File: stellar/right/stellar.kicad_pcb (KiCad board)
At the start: 2 copper layers, 158 x 119.2 mm, 100 parts, among them J1 Battery+, J2 Battery, J3 Battery-, J4 OLED, SW1 SW_Push_45deg, SW10 SW_Push_45deg, SW11 SW_Push_45deg, SW12 SW_Push_45deg, SW13 SW_Push_45deg, SW14 SW_Push_45deg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

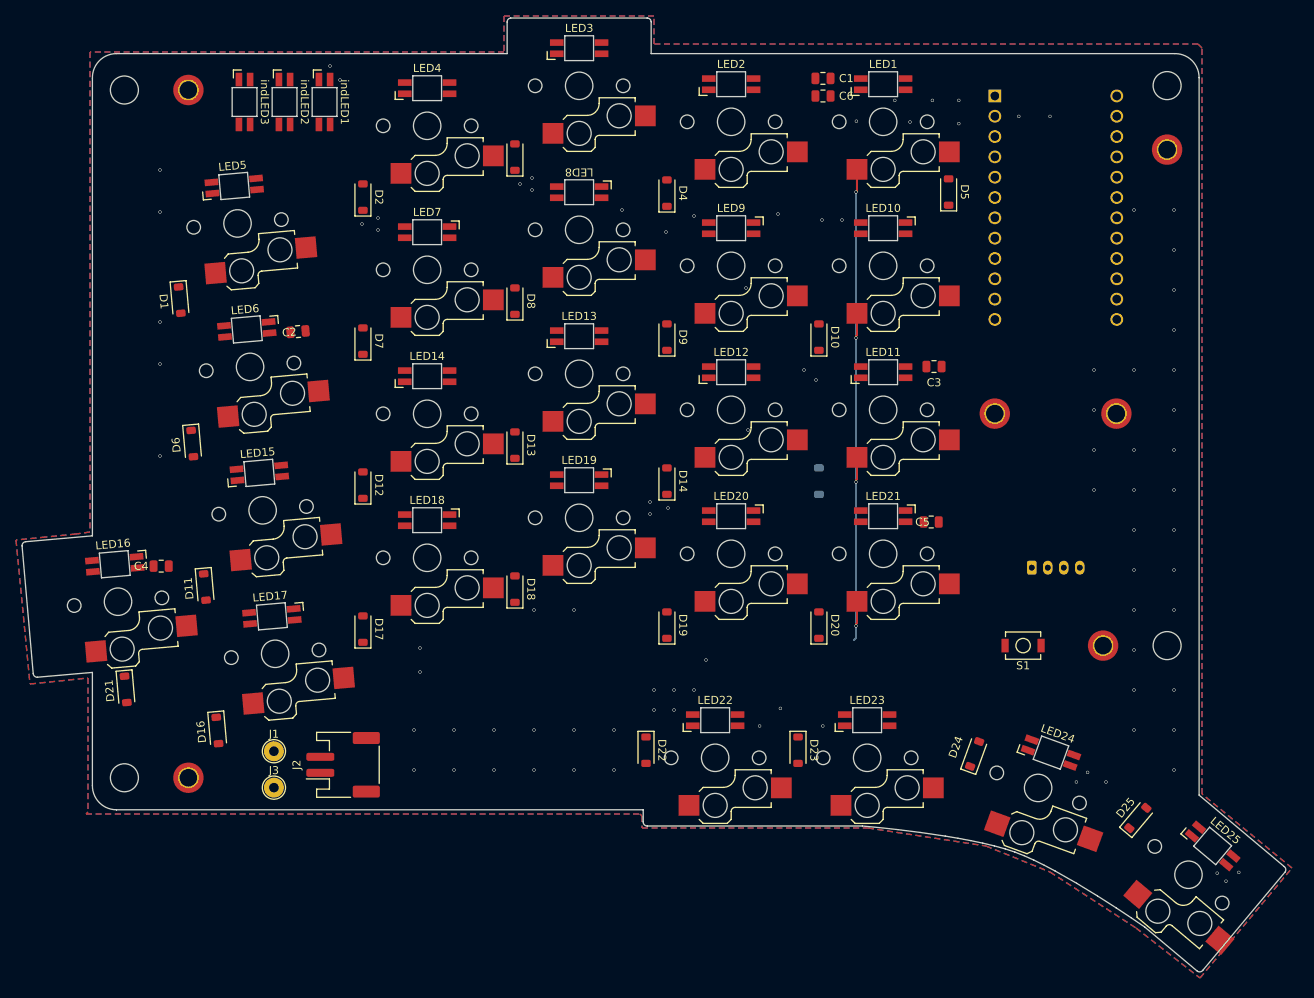
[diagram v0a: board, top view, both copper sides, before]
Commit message: [pcb] right half layout done
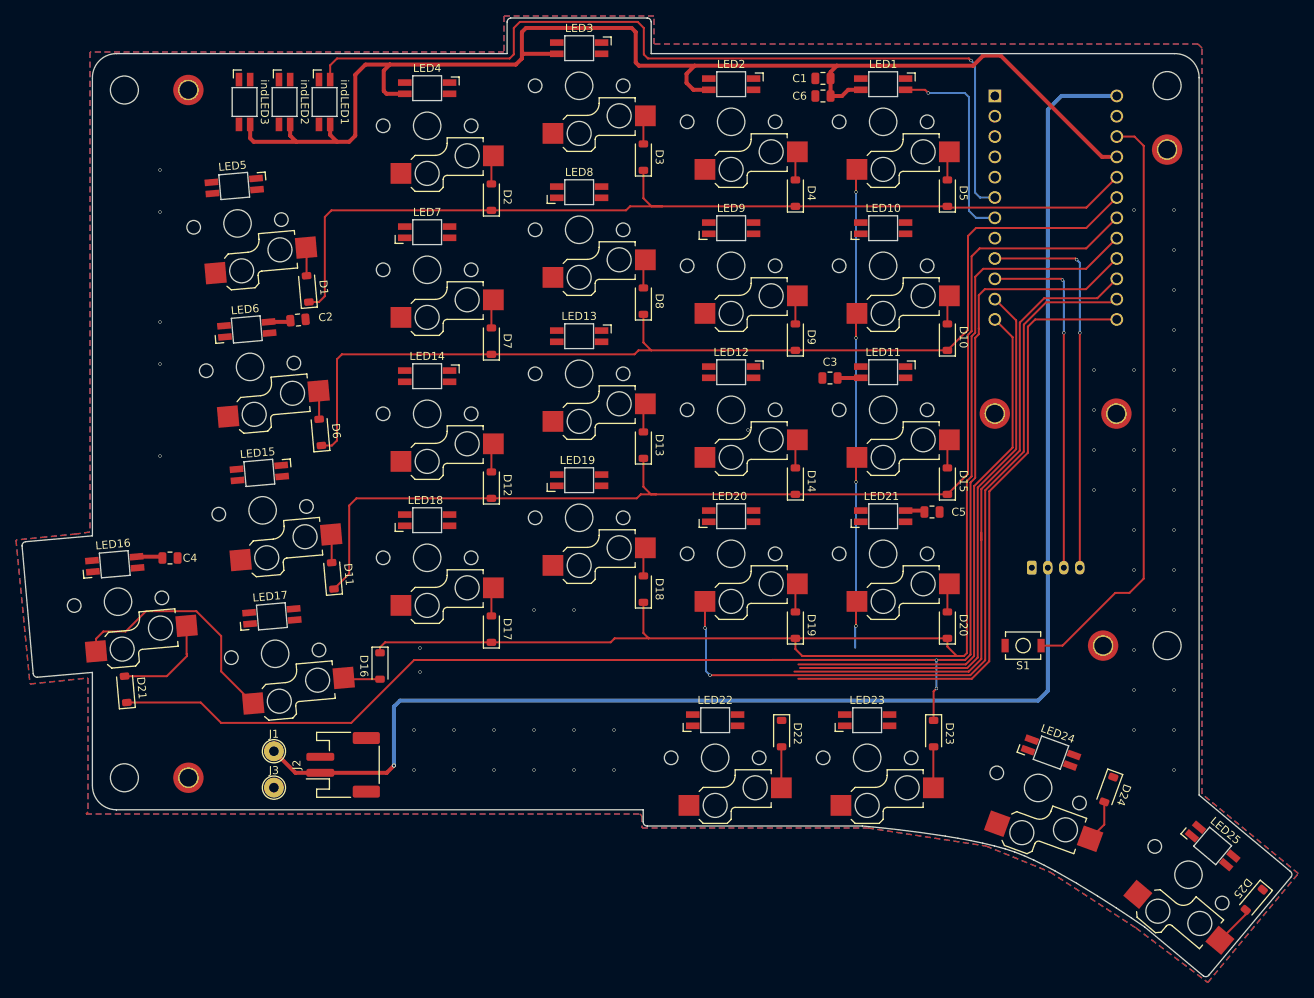
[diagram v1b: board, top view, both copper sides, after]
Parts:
- D15: moved to F.Cu
- moved D16 21.9 mm to (113.2, 114.3), turned to -90 degrees
- moved D25 17.8 mm to (222.4, 143.5), turned to -130 degrees
- moved D24 17.3 mm to (204.3, 129.8), turned to -110 degrees
- moved D22 17.1 mm to (163.4, 122.8)
- moved D23 17.1 mm to (182.4, 122.8)
- moved D10 16.1 mm to (184.1, 73.2)
- moved D12 16.1 mm to (127.1, 91.7)
- moved D13 16.1 mm to (146.1, 86.7)
- moved D14 16.1 mm to (165.1, 91.2)
- moved D15 16.1 mm to (184.1, 91.2)
- moved D17 16.1 mm to (127.1, 109.7)
- moved D18 16.1 mm to (146.1, 104.7)
- moved D19 16.1 mm to (165.1, 109.2)
- moved D2 16.1 mm to (127.1, 55.7)
- moved D20 16.1 mm to (184.1, 109.2)
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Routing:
- net +BATT: track 0.00 -> 188.4 mm, vias 0 -> 1
- net /keyscan_row4: track 0.00 -> 182.3 mm, vias 0 -> 2
- net +3V3: track 0.00 -> 173.7 mm
- net /keyscan_row3: track 0.00 -> 170.0 mm
- net /keyscan_row2: track 0.00 -> 143.2 mm
- net /keyscan_row1: track 0.00 -> 130.0 mm
- net /keyscan_row0: track 0.00 -> 119.6 mm
- net /ledin_indicators: track 0.00 -> 109.5 mm, vias 0 -> 1
- net /keyscan_column3: track 0.00 -> 101.6 mm, vias 0 -> 2
- net /keyscan_column0: track 0.00 -> 97.4 mm
- net /keyscan_column4: track 68.4 -> 152.7 mm
- net /keyscan_column2: track 0.00 -> 80.1 mm
- net Net-(U1-RESET): track 0.00 -> 74.2 mm
- net /keyscan_column1: track 0.00 -> 70.7 mm
- net /SDA: track 0.00 -> 49.0 mm, vias 0 -> 2
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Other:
- board size 158 x 119.2 mm -> 158.7 x 119.8 mm

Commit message: [pcb] right halve, more routing
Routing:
- net +3V3: track 173.7 -> 643.3 mm, vias 0 -> 26
- net /keyscan_column1: track 70.7 -> 188.9 mm, vias 0 -> 5
- net /keyscan_column2: track 80.1 -> 186.7 mm, vias 0 -> 5
- net /keyscan_column3: track 101.6 -> 164.5 mm, vias 2 -> 6
- net /keyscan_column0: track 97.4 -> 158.3 mm, vias 0 -> 4
- net Net-(LED22-DOUT): track 0.00 -> 15.0 mm
- net Net-(indLED1-DOUT): track 0.00 -> 8.70 mm
- net Net-(indLED2-DOUT): track 0.00 -> 8.56 mm
- net /keyscan_column4: track 152.7 -> 155.7 mm, vias 4 -> 5
- net GND: vias 50 -> 49

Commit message: [pcb] final version, maybe
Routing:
- net /keyscan_column0: track 158.3 -> 244.0 mm, vias 4 -> 5
- net /keyscan_row4: track 182.5 -> 256.0 mm, vias 2 -> 5
- net Net-(LED21-DOUT): track 0.00 -> 49.0 mm, vias 0 -> 2
- net /keyscan_column1: track 188.9 -> 235.6 mm
- net /keyscan_column4: track 155.7 -> 192.3 mm, vias 5 -> 7
- net Net-(LED6-DOUT): track 0.00 -> 29.7 mm
- net Net-(LED4-DOUT): track 0.00 -> 27.1 mm
- net Net-(LED14-DOUT): track 0.00 -> 27.0 mm
- net /Backlight/ledout2: track 0.00 -> 26.9 mm
- net /Backlight/ledout0: track 0.00 -> 26.8 mm
- net Net-(LED17-DOUT): track 0.00 -> 24.9 mm
- net /keyscan_column2: track 186.7 -> 208.2 mm
- net Net-(LED24-DOUT): track 0.00 -> 20.9 mm
- net /Backlight/ledout1: track 0.00 -> 20.8 mm, vias 0 -> 2
- net /keyscan_column3: track 164.5 -> 183.7 mm, vias 6 -> 7
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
